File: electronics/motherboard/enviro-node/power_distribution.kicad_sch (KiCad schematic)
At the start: 54 parts, among them J10 2604-3102, J7 2604-3102, J8 SOLAR_CRNT_JMPR, J9 BAT_CRNT_JMPR, U10 XC6215B332MR-G, U4 INA219BxD, U5 LT3652IMSE, U6 TPS22967DSGR, U7 MCP73832-2-OT, U8 INA219BxD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

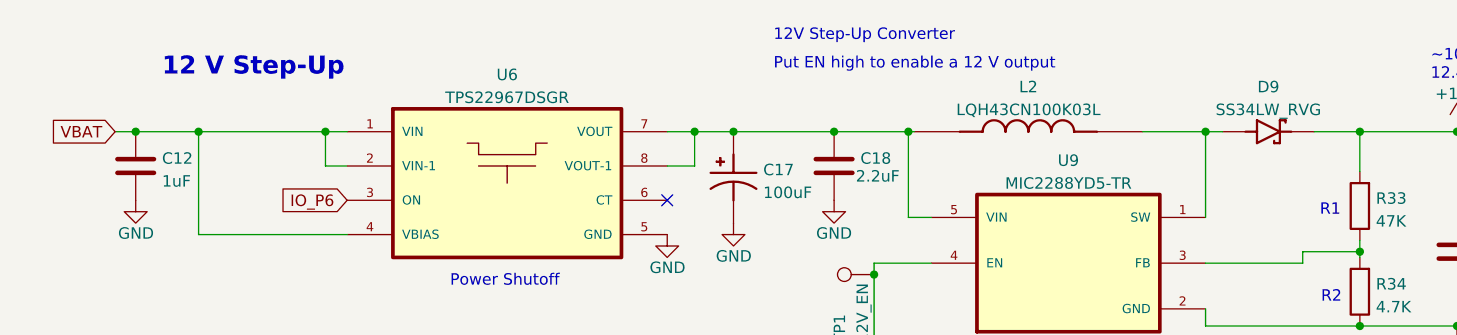
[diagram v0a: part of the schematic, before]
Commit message: fixed unexposed copper pad on inductor and added zipped step file of the motherboard
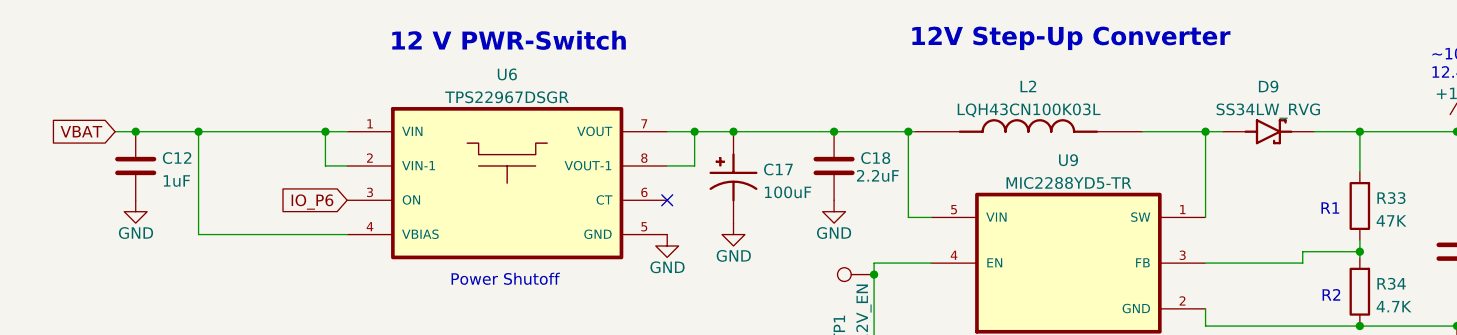
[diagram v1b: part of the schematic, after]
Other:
- note added: "12 V PWR-Switch"
- note removed: "12 V Step-Up"
- note removed: "Put EN high to enable a 12 V output"
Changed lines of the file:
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@@
     (effects (font (size 2 2) (thickness 0.4) bold) (justify left bottom))
   )
-  (text "12 V Step-Up" (at 226.314 54.61 0)
+  (text "12 V PWR-Switch\n" (at 251.587 51.943 0)
     (effects (font (size 2 2) (thickness 0.4) bold) (justify left bottom))
   )
@@
   )
   (text "Battery V & I\nMonitoring\nI2C = 0x45" (at 214.376 125.603 0)
-    (effects (font (size 1.27 1.27)) (justify left bottom))
-  )
-  (text "12V Step-Up Converter" (at 294.259 50.673 0)
     (effects (font (size 1.27 1.27)) (justify left bottom))
   )
@@
     (effects (font (size 1.27 1.27)) (justify right bottom))
   )
-  (text "Put EN high to enable a 12 V output" (at 294.259 53.848 0)
-    (effects (font (size 1.27 1.27)) (justify left bottom))
-  )
   (text "Vout = 1.24 x ((R1 / R2) + 1)\nVout = 12.4 V" (at 333.629 89.789 0)
     (effects (font (size 1.27 1.27)) (justify left bottom))
@@
     (effects (font (size 1.27 1.27)) (justify left bottom))
   )
+  (text "12V Step-Up Converter" (at 309.372 51.435 0)
+    (effects (font (size 2 2) (thickness 0.4) bold) (justify left bottom))
+  )
   (text "Solar Input" (at 48.26 150.368 0)

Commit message: updated electronics for production
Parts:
- R20, R24, R25: value 4.7K -> 2K
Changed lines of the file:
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@@
       (effects (font (size 1.27 1.27)) (justify left))
     )
-    (property "Value" "4.7K" (id 1) (at 76.454 171.8822 0)
+    (property "Value" "2K" (id 1) (at 76.454 171.8822 0)
       (effects (font (size 1.27 1.27)) (justify left))
     )
@@
     (in_bom yes) (on_board yes) (fields_autoplaced)
     (property "Reference" "R24" (id 0) (at 143.129 195.3092 90))
-    (property "Value" "4.7K" (id 1) (at 143.129 197.8461 90))
+    (property "Value" "2K" (id 1) (at 143.129 197.8461 90))
     (property "Footprint" "Resistor_SMD:R_0805_2012Metric" (id 2) (at 143.129 201.803 90)
       (effects (font (size 1.27 1.27)) hide)
@@
     (in_bom yes) (on_board yes) (fields_autoplaced)
     (property "Reference" "R25" (id 0) (at 143.383 207.1202 90))
-    (property "Value" "4.7K" (id 1) (at 143.383 209.6571 90))
+    (property "Value" "2K" (id 1) (at 143.383 209.6571 90))
     (property "Footprint" "Resistor_SMD:R_0805_2012Metric" (id 2) (at 143.383 213.614 90)
       (effects (font (size 1.27 1.27)) hide)

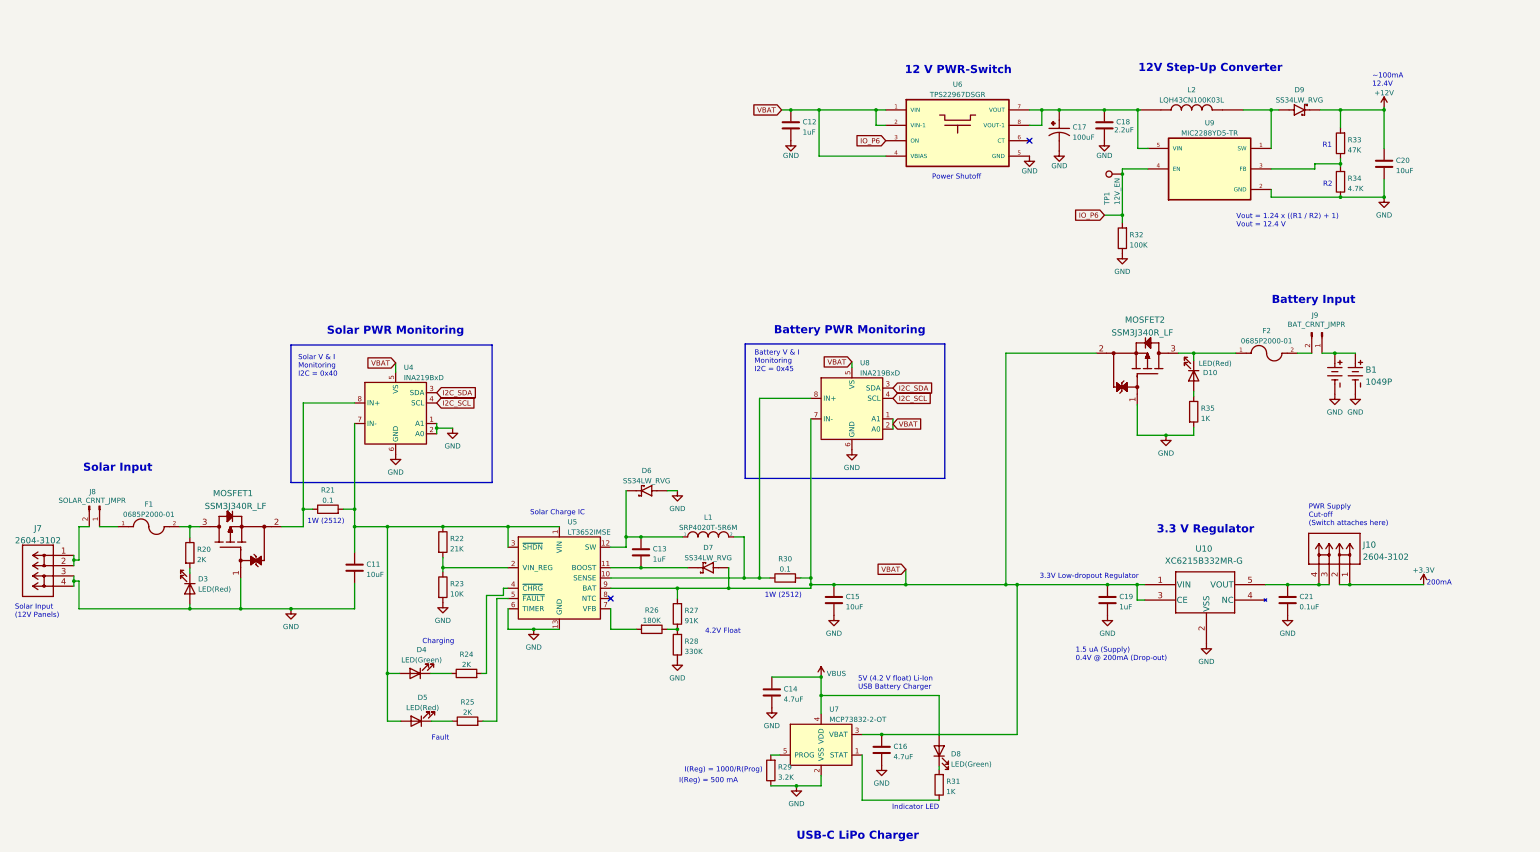
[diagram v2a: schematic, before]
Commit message: Fixed most errors on the 1.0.1 board revision, resolved ERC errors. No PCB work in this commit.
1. Added a solder jumper in-line with with the USB/UART bridge TX pin. If this jumper is
   broken then the RX pin on the UART header can be used. Note the TX/RX discrepancy here is
   not a typo.

2. Changed the USB/UART bridge power supply wiring so it will not try to power the board
   when a USB cable is plugged in. Batteries must be present.

3. The battery monitor VS/A0/A1 pins put back to +3.3v rather than VBAT so it can be read
   while the battery is being charged via the solar panel.

4. Moved the main 3.3v regulator to after the power switch so it is not running all the time.

5. Reverted the change that swapped the piezo buzzer and rain gauge input pins.

6. Noted that R42 and R43 should not be populated during manufacture.

7. Changed the part number for the USB-C LiPo charger to MCP73832T-2ACI/OT.

8. Resolved all KiCAD ERC errors on the schematics. These were all related to KiCAD not
   knowing where power was coming from or IC power pins not being correctly defined in
   the components. Warnings were not checked.
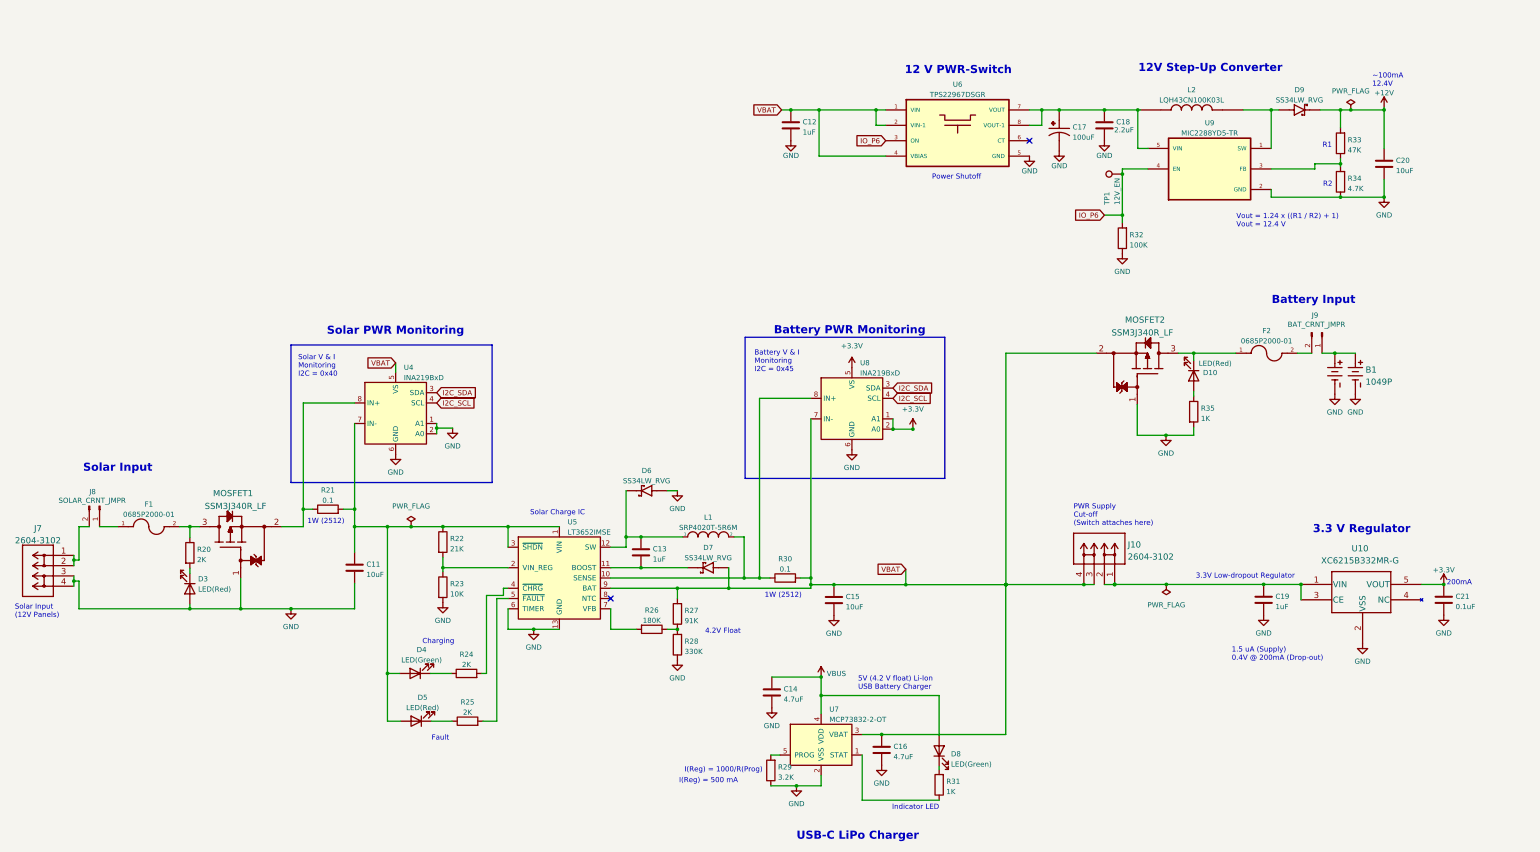
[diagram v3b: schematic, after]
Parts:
- U7: Part MCP73832-2ATI/MC -> MCP73832T-2ACI/OT
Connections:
- net +3.3V: now also C21.1, U10.5 (VOUT), U8.1 (A1), U8.2 (A0), U8.5 (VS); no longer J10.1, J10.2
- net VBAT: now also J10.3, J10.4; no longer C19.2, U10.1 (VIN), U10.3 (CE), U8.1 (A1), U8.2 (A0), U8.5 (VS)
- new net: C19.2, J10.1, J10.2, U10.1 (VIN), U10.3 (CE)
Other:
- moved on the sheet: C19, C21, J10, U10

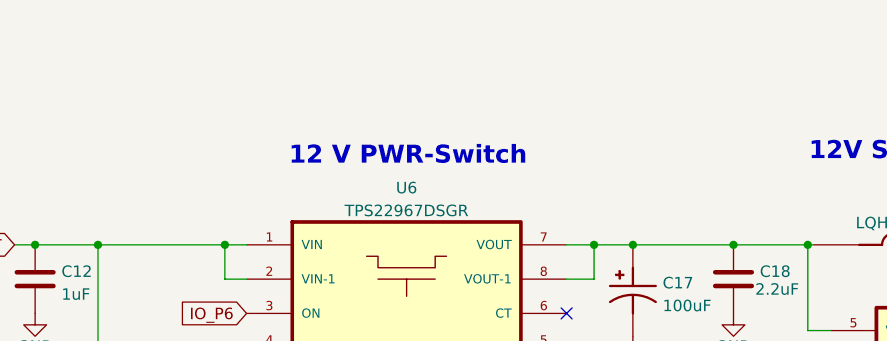
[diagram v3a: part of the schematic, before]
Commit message: Updated schematic date and revision number. Removed individual designer names because the whole team is involved now.
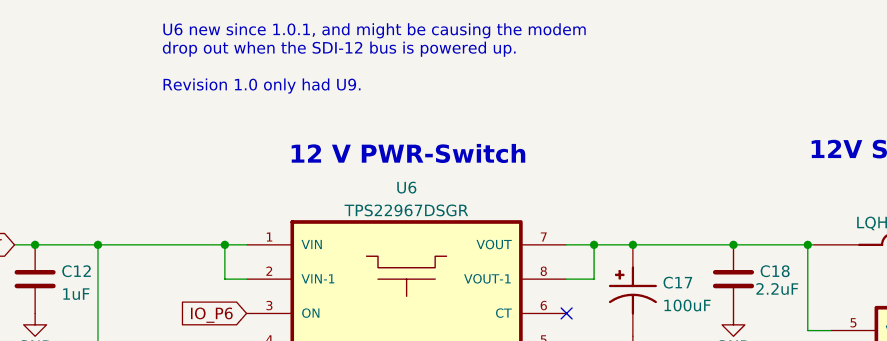
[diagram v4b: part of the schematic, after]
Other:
- note added: "U6 new since 1.0.1, and might be causing the modem drop out when the SDI-12 bus is powered up. Revision 1.0 only had U9."
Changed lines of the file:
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@@
   (title_block
     (title "Enviro-node")
-    (date "2023-01-09")
-    (rev "1.0")
+    (date "2023-04-13")
+    (rev "1.0.2")
     (company "NSW Department of Primary Industries")
     (comment 1 "GitHub: https://github.com/DPIclimate/enviro-node")
-    (comment 2 "Designed by: Harvey Bates")
   )
   (junction (at 358.013 120.777) (diameter 0) (color 0 0 0 0)
@@
     (effects (font (size 1.27 1.27)) (justify left bottom))
   )
+  (text "U6 new since 1.0.1, and might be causing the modem\ndrop out when the SDI-12 bus is powered up.\n\nRevision 1.0 only had U9."
+    (at 237.49 43.815 0)
+    (effects (font (size 1.27 1.27)) (justify left bottom))
+  )

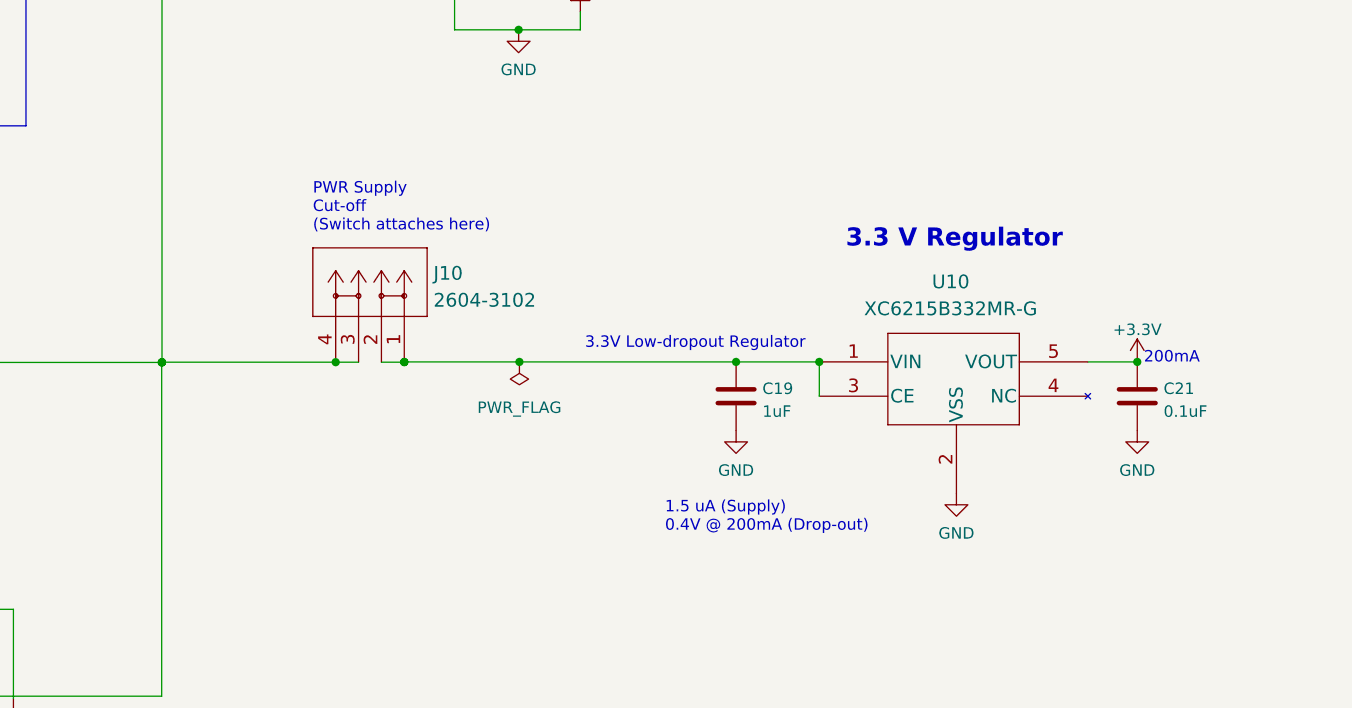
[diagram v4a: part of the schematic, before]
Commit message: Moved +3.3v regulator back to battery side of switch to reduce PCB layout work.
Replaced C17 & C23 with 0.1uF caps to adhere to datasheet recommendations.

All schematic changes put onto the PCB.
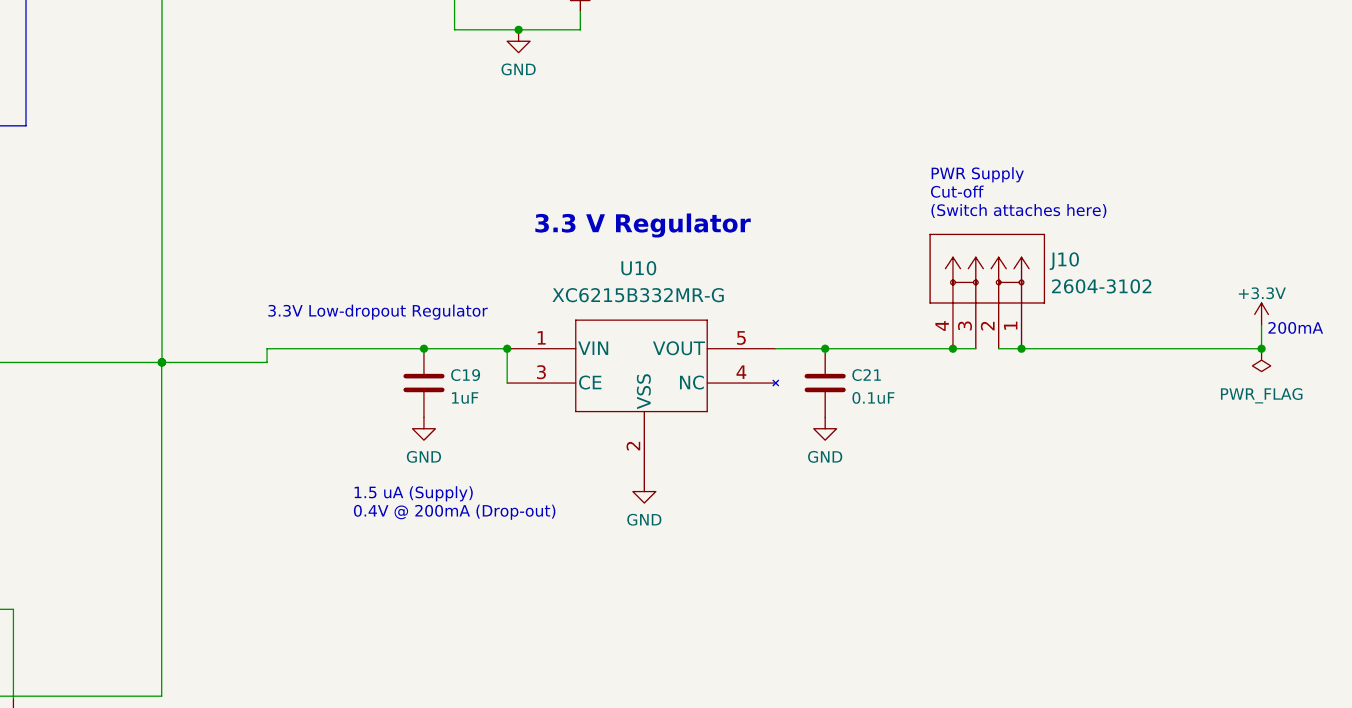
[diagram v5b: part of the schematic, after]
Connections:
- net +3.3V: now also J10.1, J10.2; no longer C21.1, U10.5 (VOUT)
- net VBAT: now also C19.2, U10.1 (VIN), U10.3 (CE); no longer J10.3, J10.4
- new net: C21.1, J10.3, J10.4, U10.5 (VOUT)
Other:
- moved on the sheet: C19, C21, J10, U10

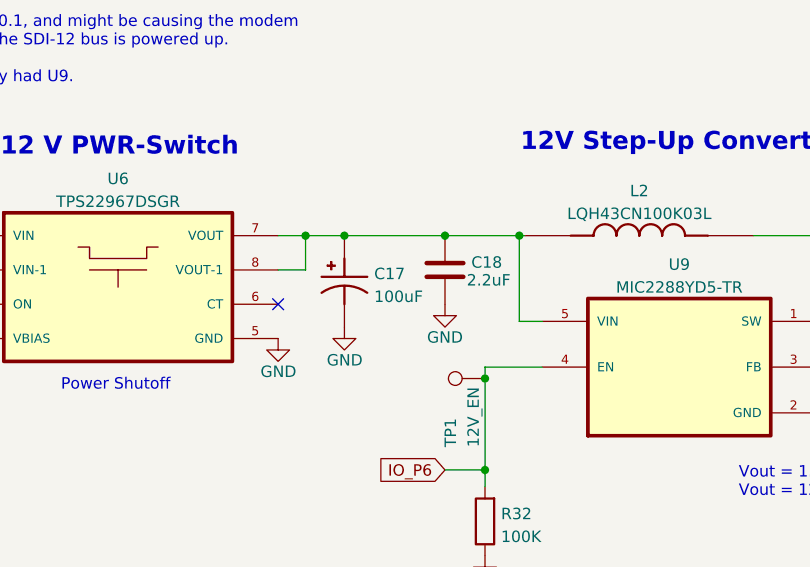
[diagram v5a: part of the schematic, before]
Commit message: Last commit did not get changes to C17 & C23, changed them again to 0.1uF.
Changed footprint of optional pull-up/pull-down R42 & R43 to be through-hole.
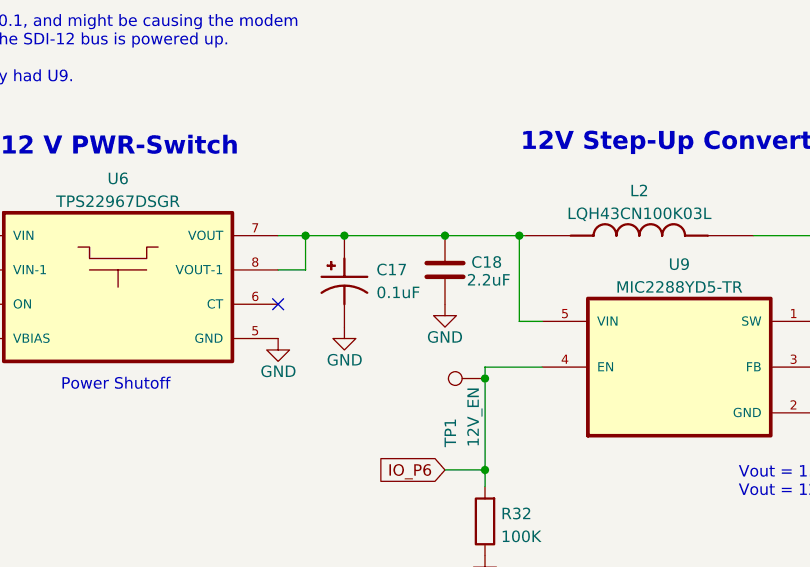
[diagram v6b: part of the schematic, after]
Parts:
- C17: value 100uF -> 0.1uF; footprint T520B107M006ATE015:CAPPM3528X210N -> Capacitor_Tantalum_SMD:CP_EIA-2012-12_Kemet-R; MANUFACTURER KEMET -> KYOCERA-AVX; Part T520B107M006ATE015 -> TAJR104K020RNJ
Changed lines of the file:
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@@
   (symbol (lib_id "T520B107M006ATE015:T520B107M006ATE015") (at 289.814 65.659 270) (unit 1)
     (in_bom yes) (on_board yes) (fields_autoplaced)
-    (property "Reference" "C17" (id 0) (at 293.116 64.8243 90)
+    (property "Reference" "C17" (id 0) (at 293.37 64.3889 90)
       (effects (font (size 1.27 1.27)) (justify left))
     )
-    (property "Value" "100uF" (id 1) (at 293.116 67.3612 90)
+    (property "Value" "0.1uF" (id 1) (at 293.37 66.9289 90)
       (effects (font (size 1.27 1.27)) (justify left))
     )
-    (property "Footprint" "T520B107M006ATE015:CAPPM3528X210N" (id 2) (at 289.814 65.659 0)
+    (property "Footprint" "Capacitor_Tantalum_SMD:CP_EIA-2012-12_Kemet-R" (id 2) (at 289.814 65.659 0)
       (effects (font (size 1.27 1.27)) (justify left bottom) hide)
     )
-    (property "Datasheet" "https://www.digikey.com.au/en/products/detail/kemet/T520B107M006ATE015/1842096?s=N4IgTCBcDaICoFYwAYBCBGZB2Ass5AbAIJwCiy6CIAugL5A" (id 3) (at 289.814 65.659 0)
+    (property "Datasheet" "https://datasheets.kyocera-avx.com/TAJ.pdf" (id 3) (at 289.814 65.659 0)
       (effects (font (size 1.27 1.27)) (justify left bottom) hide)
     )
@@
       (effects (font (size 1.27 1.27)) (justify left bottom) hide)
     )
-    (property "MANUFACTURER" "KEMET" (id 5) (at 289.814 65.659 0)
+    (property "MANUFACTURER" "KYOCERA-AVX" (id 5) (at 289.814 65.659 0)
       (effects (font (size 1.27 1.27)) (justify left bottom) hide)
     )
-    (property "Part" "T520B107M006ATE015" (id 6) (at 289.814 65.659 90)
+    (property "Part" "TAJR104K020RNJ" (id 6) (at 289.814 65.659 90)
       (effects (font (size 1.27 1.27)) hide)
     )
